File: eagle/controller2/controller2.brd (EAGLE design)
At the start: 63.5 x 63.5 mm, 45 parts, among them U1 ATMEGA328P_PDIP, X1 STEREOJACK

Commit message: controller2: eagle layout nearly finished
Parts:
- removed Q4: (no value), SparkFun-DiscreteSemi:TO-92
- removed VD1, VD2, VD3, VD4, VD5, VD6, VD7, VD8: (no value), SparkFun-Resistors:AXIAL-0.3
- added C3: 100nF, SparkFun-Passives:CAP-PTH-SMALL
- added GND, MID, TIP, VCC: TPTP14SQ, testpad:TP14SQ
- added R4: 4.7k, SparkFun-Resistors:AXIAL-0.3
- added T_DISP: (no value), SparkFun-DiscreteSemi:TO-92
- added U2: DS18B20, SparkFun-Sensors:TO-92-AMMO
- added VD11, VD12, VD21, VD22, VD31, VD32, VD41, VD42: (no value), SparkFun-Resistors:AXIAL-0.3
- C1: value (none) -> 100nF
- C2: value (none) -> 4700uF
- PWR_BATT, PWR_CAM: device SparkFun-Connectors:POWER_JACK_PTH -> SparkFun-Connectors:POWER_JACK_PTH_BREAD
- R3: value (none) -> 10k
- moved Q5 51.4 mm to (71.1, 48.3), turned to 0 degrees
- moved CONV_X_75V 38.8 mm to (12.7, 50.8)
- moved J1 37.6 mm to (20.3, 14.0)
- moved H4 14.0 mm to (5.08, 5.08)
- moved C2 12.7 mm to (22.9, 33.0), turned to 90 degrees
- moved X1 7.62 mm to (0.00, 15.2)
- moved Q2 5.24 mm to (21.6, 41.9), turned to 0 degrees
- moved 3.3V 2.54 mm to (16.5, 10.2)
- moved CONV_X_VCC 1.27 mm to (59.7, 50.8)
- moved Q3 1.27 mm to (33.0, 59.7)
- moved BTN_DW 1.27 mm to (58.4, 15.2), turned to 90 degrees
- moved BTN_UP 1.27 mm to (58.4, 24.1), turned to 90 degrees
- moved BTN_X 1.27 mm to (58.4, 6.35), turned to 90 degrees
- moved SHTR_BRKOUT 1.27 mm to (14.0, 21.6)
- renumbered Q1 to T_ZERO, Y1 to RES
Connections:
- removed net FOO4: U1.13
- removed net FOO9: U1.14
- new net N$13: TIP.TP, X1.4
- new net N$14: MID.TP, X1.3
- new net TEMP: R4.P$1, U1.14, U2.2
- net CELL1: now also VD11.P$1, VD12.P$2; no longer VD1.P$1, VD2.P$2
- net CELL2: now also VD21.P$1, VD22.P$2; no longer VD3.P$1, VD4.P$2
- net CELL3: now also VD31.P$1, VD32.P$2; no longer VD5.P$1, VD6.P$2
- net CELL4: now also VD41.P$1, VD42.P$2; no longer VD7.P$1, VD8.P$2
- net DISP_EN: now also T_DISP.2; no longer Q4.2
- net DISP_RST: now also U1.13
- net GND: now also C3.1, GND.TP, Q3.2, RES.2, T_DISP.1, U2.1, VD12.P$1, VD22.P$1, VD32.P$1, VD42.P$1; no longer Q4.1, VD2.P$1, VD4.P$1, VD6.P$1, VD8.P$1
- net N$10: now also VD31.P$2; no longer VD5.P$2
- net N$11: now also VD41.P$2; no longer VD7.P$2
- net N$3: now also T_DISP.3; no longer Q4.3
- net N$4: now also VD11.P$2; no longer VD1.P$2
- net N$5: now also VD21.P$2; no longer VD3.P$2
- net VCC: now also C3.2, R4.P$2, U2.3, VCC.TP
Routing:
- net DISP_RST: track 0.00 -> 66.6 mm
- net VCC: track 105.5 -> 158.2 mm
- net BATT_VCC: track 108.0 -> 72.7 mm
- net CELL3: track 41.0 -> 10.5 mm
- net CELL4: track 41.0 -> 14.1 mm
- net CELL1: track 38.1 -> 12.4 mm
- net CAM_VCC: track 57.4 -> 42.5 mm
- net TEMP: track 0.00 -> 13.8 mm
- net N$14: track 0.00 -> 8.51 mm
- net N$13: track 0.00 -> 6.63 mm
- net CAM_EN: track 17.1 -> 23.0 mm
- net BTN3: track 28.8 -> 34.4 mm
- net BTN2: track 37.4 -> 42.7 mm
- net CELL2: track 41.4 -> 37.2 mm
- net BTN1: track 52.5 -> 50.0 mm
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
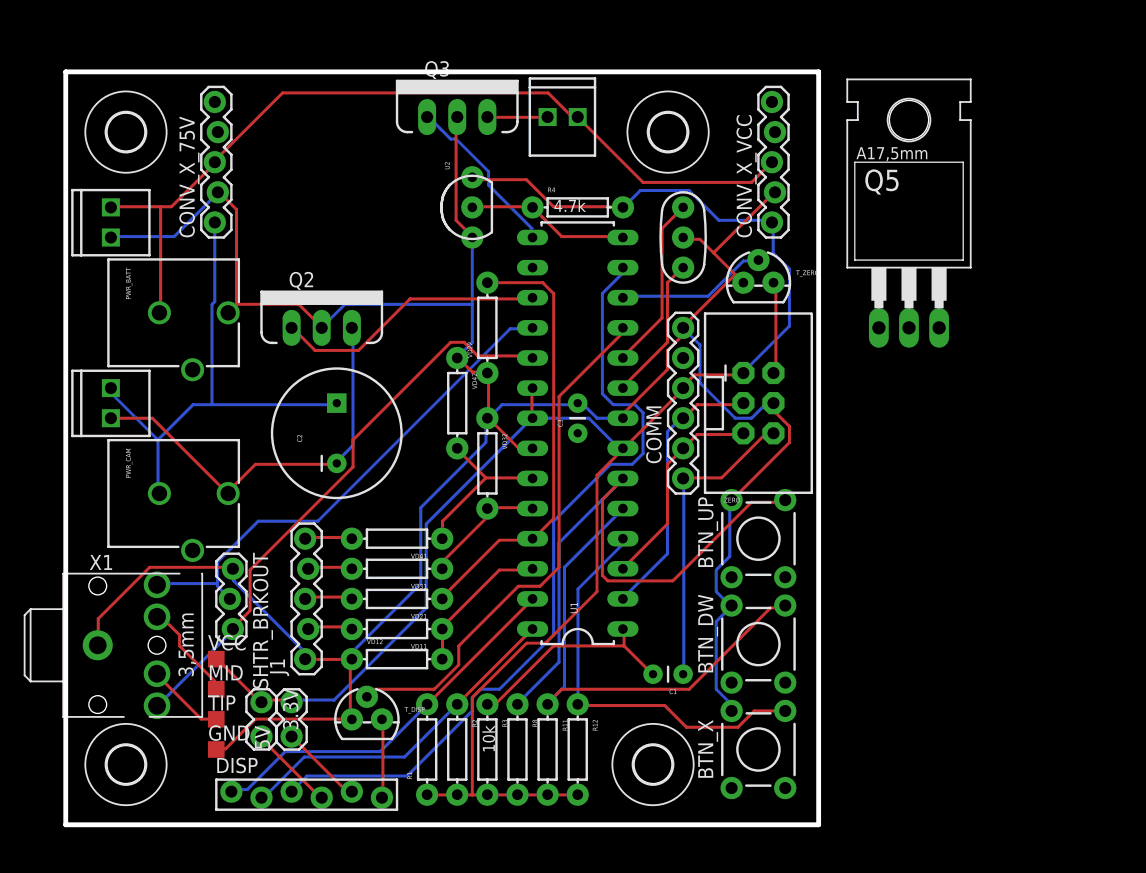
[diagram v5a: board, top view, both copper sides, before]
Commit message: controller2: net classes for power supply lines
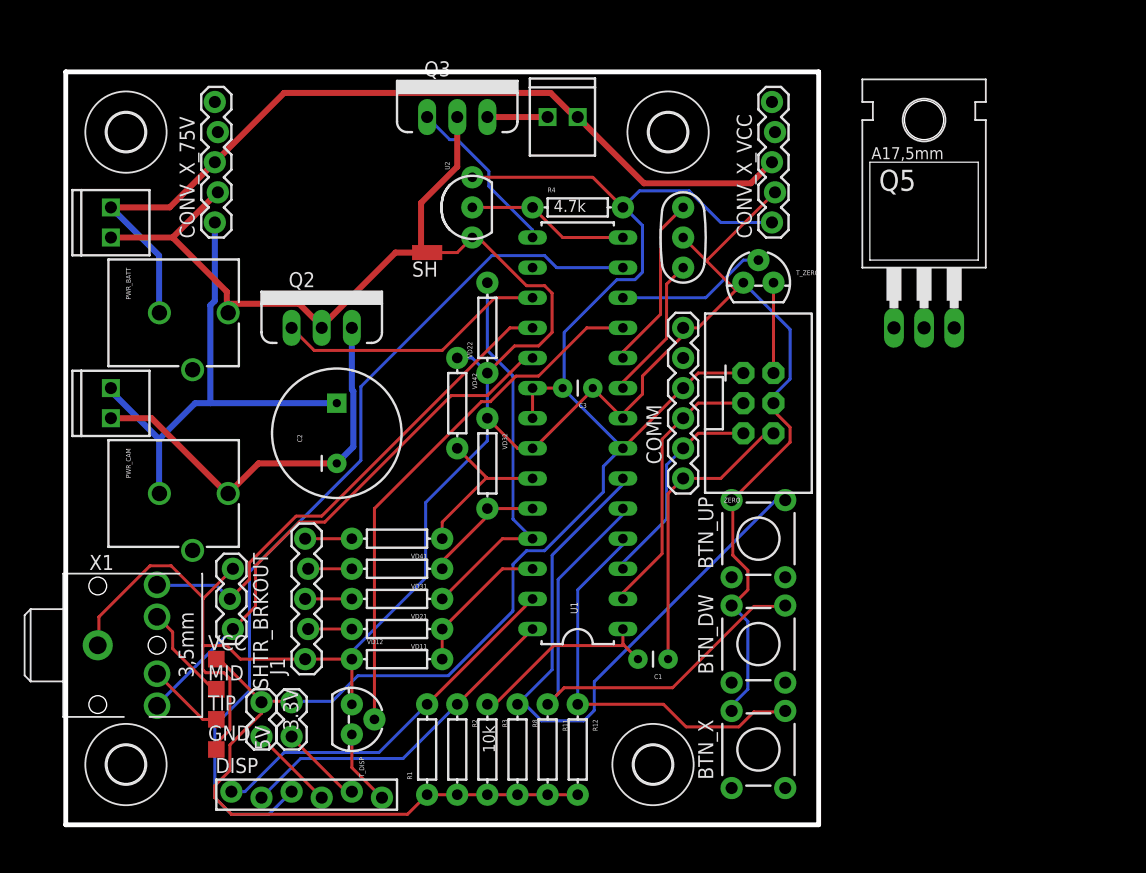
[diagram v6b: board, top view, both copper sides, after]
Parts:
- added SH: SHORT-HT5, shorts-old:SHORT_TOP-50
- moved C3 4.02 mm to (44.5, 36.8), turned to 180 degrees
- moved C1 1.80 mm to (50.8, 14.0)
- moved T_DISP 1.27 mm to (24.1, 8.89), turned to 270 degrees
- moved Q5 1.27 mm to (72.4, 48.3)
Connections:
- new net GNDA: CONV_X_75V.2, PWR_BATT.PWR, Q2.2, Q3.2, SH.2, ST_BATT.P2
- net GND: now also SH.1; no longer CONV_X_75V.2, PWR_BATT.PWR, Q2.2, Q3.2, ST_BATT.P2
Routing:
- net GNDA: track 0.00 -> 52.2 mm
- net GND: track 235.3 -> 194.1 mm
- net DISP_RST: track 66.6 -> 74.7 mm
- net BTN1: track 50.0 -> 55.2 mm
- net VCC: track 158.2 -> 162.8 mm
- net CELL2: track 37.2 -> 32.9 mm
- net CAM1: track 48.5 -> 45.9 mm
- net N$1: track 18.5 -> 16.6 mm
- net BATT_VCC: track 72.7 -> 74.2 mm
- net CAM2: track 43.5 -> 42.5 mm
- net DISP_EN: track 44.1 -> 45.0 mm
- net RST: track 25.8 -> 25.0 mm

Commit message: controller2: routing finished
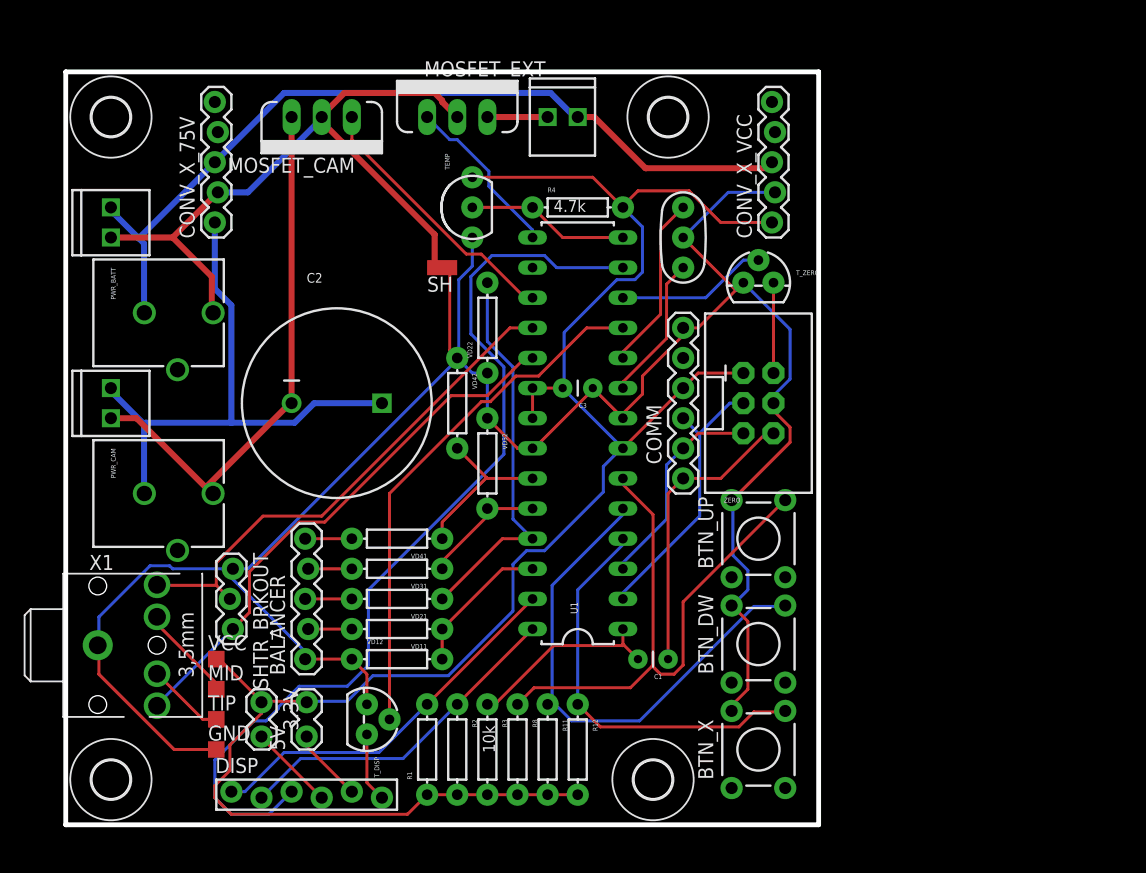
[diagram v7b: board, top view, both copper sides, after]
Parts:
- removed Q2: (no value), SparkFun-DiscreteSemi:TO220V
- removed Q5: (no value), transistor-power:TO220BH
- added MOSFET_CAM: (no value), SparkFun-DiscreteSemi:TO220V
- C2: device SparkFun-Passives:CPOL-RADIAL-1000UF-25V -> SparkFun-Passives:CPOL-RADIAL-1000UF-63V
- U1: value ATMEGA328P_PDIP -> ATMEGA328P
- X1: value STEREOJACK -> (none)
- moved C2 2.54 mm to (22.9, 35.6), turned to 0 degrees
- moved H4 1.80 mm to (3.81, 3.81)
- moved H1 1.80 mm to (3.81, 59.7)
- moved SH 1.80 mm to (31.8, 47.0)
- moved H2 1.27 mm to (49.5, 3.81)
- moved PWR_BATT 1.27 mm to (-1.27, 43.2)
- moved PWR_CAM 1.27 mm to (-1.27, 27.9)
- moved 5V 1.27 mm to (20.3, 7.62)
- moved T_DISP 1.27 mm to (25.4, 8.89)
- moved H3 1.27 mm to (50.8, 59.7)
- renumbered J1 to BALANCER, Q3 to MOSFET_EXT, ST_BATT1 to ST_EXT, U2 to TEMP
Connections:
- net CAM_EN: now also MOSFET_CAM.1; no longer Q2.1
- net CAM_OUT: now also MOSFET_CAM.3; no longer Q2.3
- net GNDA: now also MOSFET_CAM.2; no longer Q2.2
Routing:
- net CAM_OUT: track 34.8 -> 46.2 mm
- net GNDA: track 52.2 -> 59.8 mm
- net CAM_VCC: track 42.2 -> 48.3 mm
- net DISP_RST: track 74.7 -> 80.0 mm
- net BTN1: track 55.2 -> 50.3 mm
- net BATT_VCC: track 74.2 -> 71.4 mm
- net GND: track 194.1 -> 192.1 mm
- net BTN2: track 42.6 -> 44.0 mm
- net CAM2: track 42.5 -> 43.4 mm
- net N$6: track 7.05 -> 6.23 mm
- net N$3: track 6.39 -> 5.86 mm
- net DISP_EN: track 45.0 -> 44.5 mm

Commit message: controller2: silkscreen
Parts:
- renumbered SHTR_BRKOUT to SHTR
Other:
- board text added: "+"
- board text added: "1"
- board text added: "2"
- board text added: "3"
- board text added: "4"
- board text added: "7.5V"
- board text added: "GND"
- board text added: "MID"
- board text added: "RST"
- board text added: "T"
- board text added: "TIP"
- board text added: "TX"
- board text added: "VCC"
- board text added: "X"
